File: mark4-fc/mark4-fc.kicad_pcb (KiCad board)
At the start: 4 copper layers, 48 x 48 mm, 75 parts, among them J1 SWD, J2 USB_C_Receptacle_USB2.0_16P, J3 Conn_01x04, J4 Conn_01x06, J5 Conn_01x04, J6 Conn_01x08, Q1 SS8050, U1 AP63205WU, U2 TLV1117LV33, U3 STM32F722RETx, U4 LSM6DSR, U5 SPA06-003, U6 W25Q128JVSIQ, U7 USBLC6-2SC6, Y1 8MHz

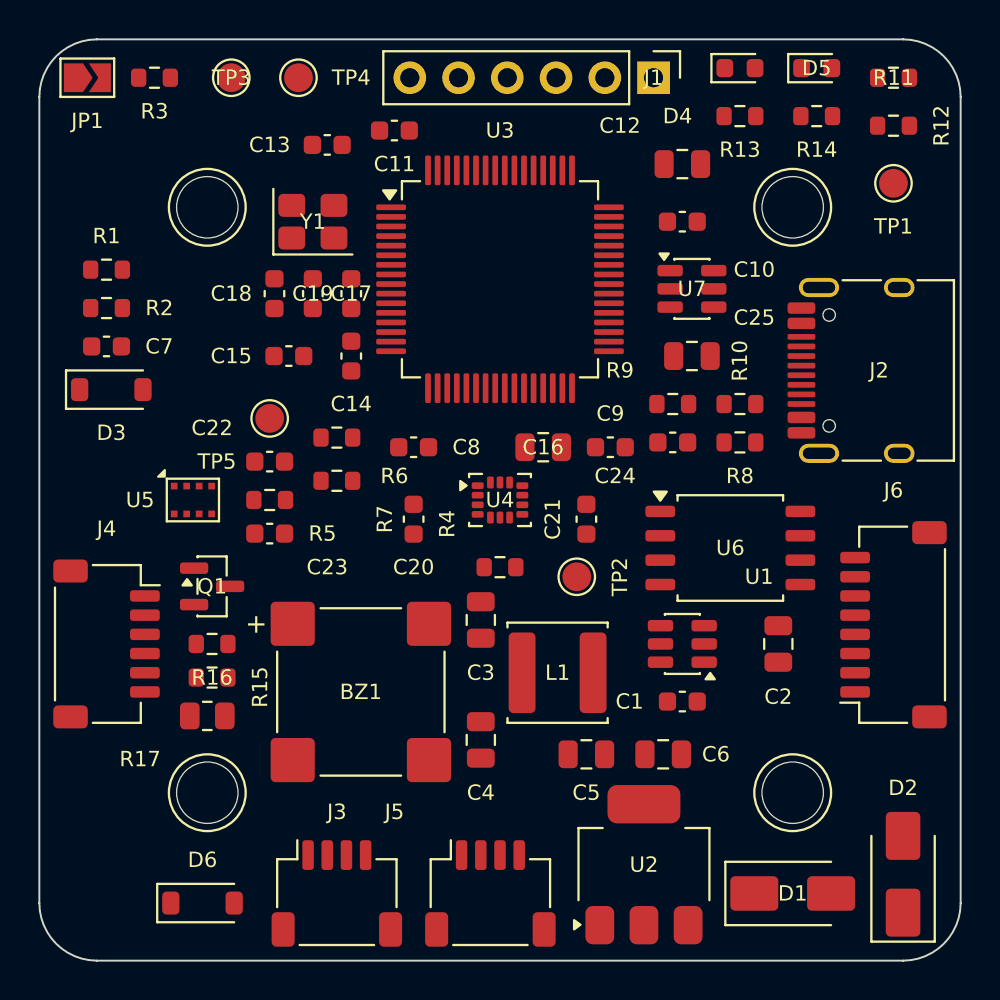
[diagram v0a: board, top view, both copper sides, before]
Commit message: feat(hardware): shrink mark4-fc to 36x36 and split assembly by side
Board outline, connectors and assembly strategy all move in one pass;
schematic, PCB and the fab package are propagated together.

- Rebuild the Edge.Cuts outline at 36x36 (the floor the 30.5 mm M3
  pattern allows) and fix the four corner fillets whose arc midpoints
  sat diametrically opposite, which cut a 4 mm disc out of each corner.
- Reduce SWD from 6 to 3 positions (SWDIO/SWCLK/GND) so SWD plus USB-C
  fit the edge budget; SWO is gone, BOOT0 stays the recovery path.
- Move the hand-soldered parts (LDO, flash, Q1, JP1, test points and
  their pull-ups) to the bottom face; the JLCPCB package now covers the
  top side only (CPL 63 -> 52, BOM 31 -> 26 lines).
- Re-relax the placement into the smaller outline with the electrically
  critical groups hand-anchored (crystal, VCAP, buck corner, connector
  ESD); LED strip pads move to the left edge to clear the USB row.
  DRC clean, schematic parity 0, nothing routed yet.
- Hide top-silk refdes and values in favour of pad labels, add the
  orientation arrow (direction still to confirm against the frame).
- Replace the footprint-family CPL rotation table with measured,
  LCSC-keyed corrections (jlcpcb-cpl-rotations.csv), derived from the
  EasyEDA footprints; fixes U2, U1 and Q1 which the community table got
  wrong or missed.
- Correct the STO-2 flash substitution note: no 256 Mbit Winbond exists
  in SOIC-8 208 mil; list the real drop-ins and the EN4B firmware cost.

Co-Authored-By: Claude Fable 5 <noreply@anthropic.com>
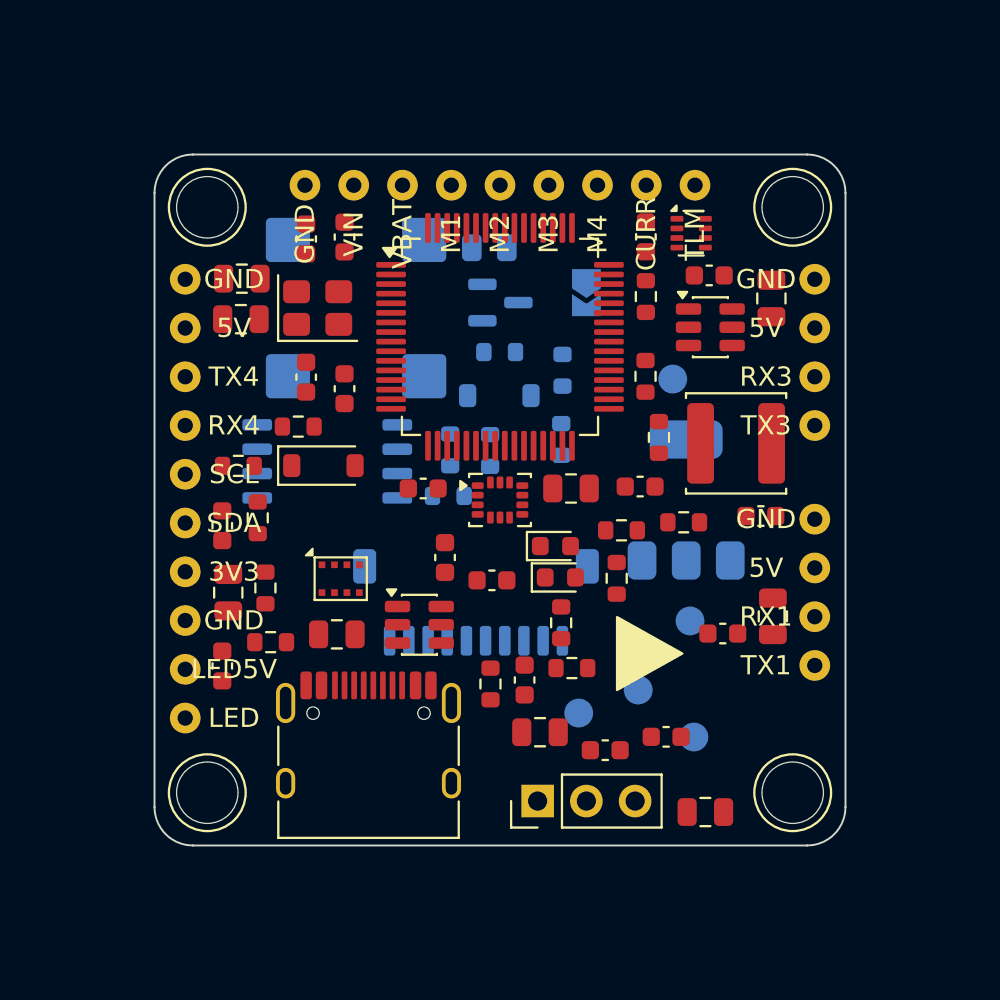
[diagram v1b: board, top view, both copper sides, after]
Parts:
- removed D1, D2: SS54, Diode_SMD:D_SMA
- removed J3, J5: Conn_01x04, Connector_JST:JST_SH_SM04B-SRSS-TB_1x04-1MP_P1.00mm_Horizontal
- removed J4: Conn_01x06, Connector_JST:JST_SH_SM06B-SRSS-TB_1x06-1MP_P1.00mm_Horizontal
- removed J6: Conn_01x08, Connector_JST:JST_SH_SM08B-SRSS-TB_1x08-1MP_P1.00mm_Horizontal
- added C26: 22uF, C_0805_2012Metric, F.Cu at (86.5, 90.6)
- added J10: GND, SolderPad_1x01_THT, F.Cu at (116.4, 101.0)
- added J11: 5V, SolderPad_1x01_THT, F.Cu at (116.4, 103.5)
- added J12: RX1, SolderPad_1x01_THT, F.Cu at (116.4, 106.1)
- added J13: TX1, SolderPad_1x01_THT, F.Cu at (116.4, 108.6)
- added J20: GND, SolderPad_1x01_THT, F.Cu at (83.6, 88.5)
- added J21: 5V, SolderPad_1x01_THT, F.Cu at (83.6, 91.0)
- added J22: TX4, SolderPad_1x01_THT, F.Cu at (83.6, 93.6)
- added J23: RX4, SolderPad_1x01_THT, F.Cu at (83.6, 96.1)
- added J24: SCL, SolderPad_1x01_THT, F.Cu at (83.6, 98.7)
- added J25: SDA, SolderPad_1x01_THT, F.Cu at (83.6, 101.2)
- added J26: 3V3, SolderPad_1x01_THT, F.Cu at (83.6, 103.7)
- added J30: GND, SolderPad_1x01_THT, F.Cu at (116.4, 88.5)
- added J31: 5V, SolderPad_1x01_THT, F.Cu at (116.4, 91.0)
- added J32: RX3, SolderPad_1x01_THT, F.Cu at (116.4, 93.6)
- added J33: TX3, SolderPad_1x01_THT, F.Cu at (116.4, 96.1)
- added J40: GND, SolderPad_1x01_THT, F.Cu at (89.8, 83.6)
- added J41: VIN, SolderPad_1x01_THT, F.Cu at (92.4, 83.6)
- added J42: VBAT, SolderPad_1x01_THT, F.Cu at (94.9, 83.6)
- added J43: M1, SolderPad_1x01_THT, F.Cu at (97.5, 83.6)
- added J44: M2, SolderPad_1x01_THT, F.Cu at (100.0, 83.6)
- added J45: M3, SolderPad_1x01_THT, F.Cu at (102.5, 83.6)
- added J46: M4, SolderPad_1x01_THT, F.Cu at (105.1, 83.6)
- added J47: CURR, SolderPad_1x01_THT, F.Cu at (107.6, 83.6)
- added J48: TLM, SolderPad_1x01_THT, F.Cu at (110.2, 83.6)
- added J50: GND, SolderPad_1x01_THT, F.Cu at (83.6, 106.3)
- added J51: LED5V, SolderPad_1x01_THT, F.Cu at (83.6, 108.8)
- added J52: LED, SolderPad_1x01_THT, F.Cu at (83.6, 111.4)
- added J7: ESC_JST_VELOX, JST_SH_SM10B-SRSS-TB_1x10-1MP_P1.00mm_Horizontal, B.Cu at (98.8, 105.3)
- added R18: 100k, R_0603_1608Metric, F.Cu at (107.6, 89.4)
- added R19: 33k, R_0603_1608Metric, F.Cu at (109.6, 101.2)
- added R20: 10k, R_0603_1608Metric, F.Cu at (108.3, 96.7)
- added R21: 330R, R_0603_1608Metric, F.Cu at (103.2, 106.4)
- added U8: TPS2116DRL, SOT-583-8, F.Cu at (110.0, 86.1)
- BZ1: footprint mark4-fc:Buzzer_MLT-8540 -> Buzzer_MLT-8540; moved to B.Cu
- C1, C10, C11, C13, C14, C15, C17, C18, C19, C20, C21, C22, C23, C24, C7, C8, C9: footprint Capacitor_SMD:C_0603_1608Metric -> C_0603_1608Metric
- C12, C2, C25, C3, C4, C5, C6: footprint Capacitor_SMD:C_0805_2012Metric -> C_0805_2012Metric
- C16: value 4.7uF ESR 0.1-0.2R -> 4.7uF; footprint Capacitor_SMD:C_0805_2012Metric -> C_0805_2012Metric
- D3: footprint Diode_SMD:D_SOD-123 -> D_SOD-123
- D4: value LED -> KT-0603R; footprint LED_SMD:LED_0603_1608Metric -> LED_0603_1608Metric
- D5: value LED -> NCD0603Y2; footprint LED_SMD:LED_0603_1608Metric -> LED_0603_1608Metric
- D6: footprint Diode_SMD:D_SOD-123 -> D_SOD-123; moved to B.Cu
- J1: footprint Connector_PinHeader_2.54mm:PinHeader_1x06_P2.54mm_Vertical -> PinHeader_1x03_P2.54mm_Vertical
- J2: footprint Connector_USB:USB_C_Receptacle_HRO_TYPE-C-31-M-12 -> USB_C_Receptacle_HRO_TYPE-C-31-M-12
- JP1: footprint Jumper:SolderJumper-2_P1.3mm_Open_TrianglePad1.0x1.5mm -> SolderJumper-2_P1.3mm_Open_TrianglePad1.0x1.5mm; moved to B.Cu
- L1: footprint mark4-fc:L_Sunlord_SWPA5040S -> L_Sunlord_SWPA5040S
- MH1, MH2, MH3, MH4: footprint mark4-fc:MountingHole_M3_3.2mm_Grommet -> MountingHole_M3_3.2mm_Grommet
- Q1: footprint Package_TO_SOT_SMD:SOT-23 -> SOT-23; moved to B.Cu
- R1: value 10k -> 100k; footprint Resistor_SMD:R_0603_1608Metric -> R_0603_1608Metric
- R10, R15, R16, R3, R8, R9: footprint Resistor_SMD:R_0603_1608Metric -> R_0603_1608Metric; moved to B.Cu
- R11, R12, R13, R14, R4, R5, R6, R7: footprint Resistor_SMD:R_0603_1608Metric -> R_0603_1608Metric
- R17: value 6R8 -> 5R1; footprint Resistor_SMD:R_0805_2012Metric -> R_0805_2012Metric; moved to B.Cu
- R2: value 1.5k -> 12k; footprint Resistor_SMD:R_0603_1608Metric -> R_0603_1608Metric
- TP1, TP2, TP3, TP4, TP5: footprint TestPoint:TestPoint_Pad_D1.5mm -> TestPoint_Pad_D1.5mm; moved to B.Cu
- U1: footprint Package_TO_SOT_SMD:TSOT-23-6 -> TSOT-23-6
- U2: footprint Package_TO_SOT_SMD:SOT-223-3_TabPin2 -> SOT-223-3_TabPin2; moved to B.Cu
- U3: footprint Package_QFP:LQFP-64_10x10mm_P0.5mm -> LQFP-64_10x10mm_P0.5mm
- U4: footprint Package_LGA:LGA-14_3x2.5mm_P0.5mm_LayoutBorder3x4y -> LGA-14_3x2.5mm_P0.5mm_LayoutBorder3x4y
- U5: footprint mark4-fc:Goertek_LGA-8_2x2.5mm_P0.65mm_ClockwisePinNumbering -> Goertek_LGA-8_2x2.5mm_P0.65mm_ClockwisePinNumbering
- U6: footprint mark4-fc:SOIC-8_5.28x5.28mm_P1.27mm -> SOIC-8_5.28x5.28mm_P1.27mm; moved to B.Cu
- U7: footprint Package_TO_SOT_SMD:SOT-23-6 -> SOT-23-6
- Y1: footprint Crystal:Crystal_SMD_3225-4Pin_3.2x2.5mm -> Crystal_SMD_3225-4Pin_3.2x2.5mm
- moved TP3 38.3 mm to (107.2, 109.9)
- moved J1 38.2 mm to (102.0, 115.7), turned to 90 degrees
- moved R12 35.9 mm to (99.5, 109.6), turned to 90 degrees
- moved R11 35.0 mm to (103.7, 108.8)
- moved TP4 34.9 mm to (109.9, 106.3)
- moved J2 33.6 mm to (93.2, 113.7), turned to 0 degrees
- moved C12 32.5 mm to (85.8, 104.8), turned to 90 degrees
- moved D6 30.6 mm to (100.0, 94.6)
- moved C5 30.6 mm to (86.5, 88.5)
- moved C13 29.7 mm to (101.3, 109.4), turned to 90 degrees
- moved R17 28.5 mm to (99.4, 86.9)
- moved D5 28.4 mm to (102.9, 102.4)
- moved R3 28.4 mm to (103.2, 96.8), turned to -90 degrees
- moved JP1 28.3 mm to (104.5, 89.2), turned to -90 degrees
- moved R2 28.3 mm to (107.6, 93.6), turned to 90 degrees
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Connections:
- net /12V_SENSE renamed /VBAT_SENSE
- net /Power/5V_BUCK renamed +5V_BUCK
- C2 pad 1: +12V -> +10V
- J1 pad 1: +3V3 -> /MCU/SWDIO
- R1 pad 1: +12V -> VBAT
- U1 pad 2: +12V -> +10V
- U1 pad 3: +12V -> +10V
- U3 pad 43: unconnected-(U3-PA10-Pad43) -> /LED_DATA
- U3 pad 53: unconnected-(U3-PC12-Pad53) -> /PWR_SRC
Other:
- board size 48 x 48 mm -> 36 x 36 mm
